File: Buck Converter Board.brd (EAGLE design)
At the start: 132.3 x 52 mm, 14 parts, among them J2 POWERPOLE_POWER25A_HORIZONTAL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, J3 POWERPOLE_POWER25A_HORIZONTAL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

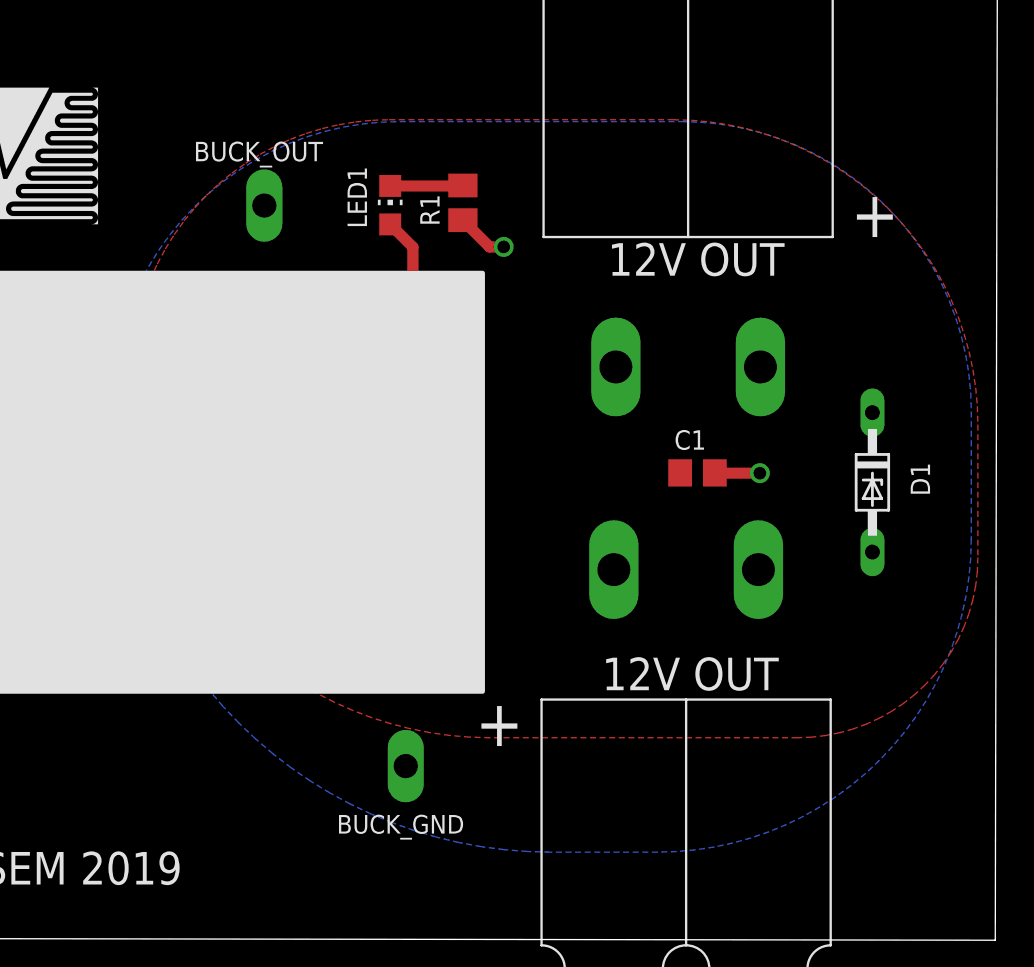
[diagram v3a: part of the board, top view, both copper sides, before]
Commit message: changed bypass cap on 555 to 22uF panasonic
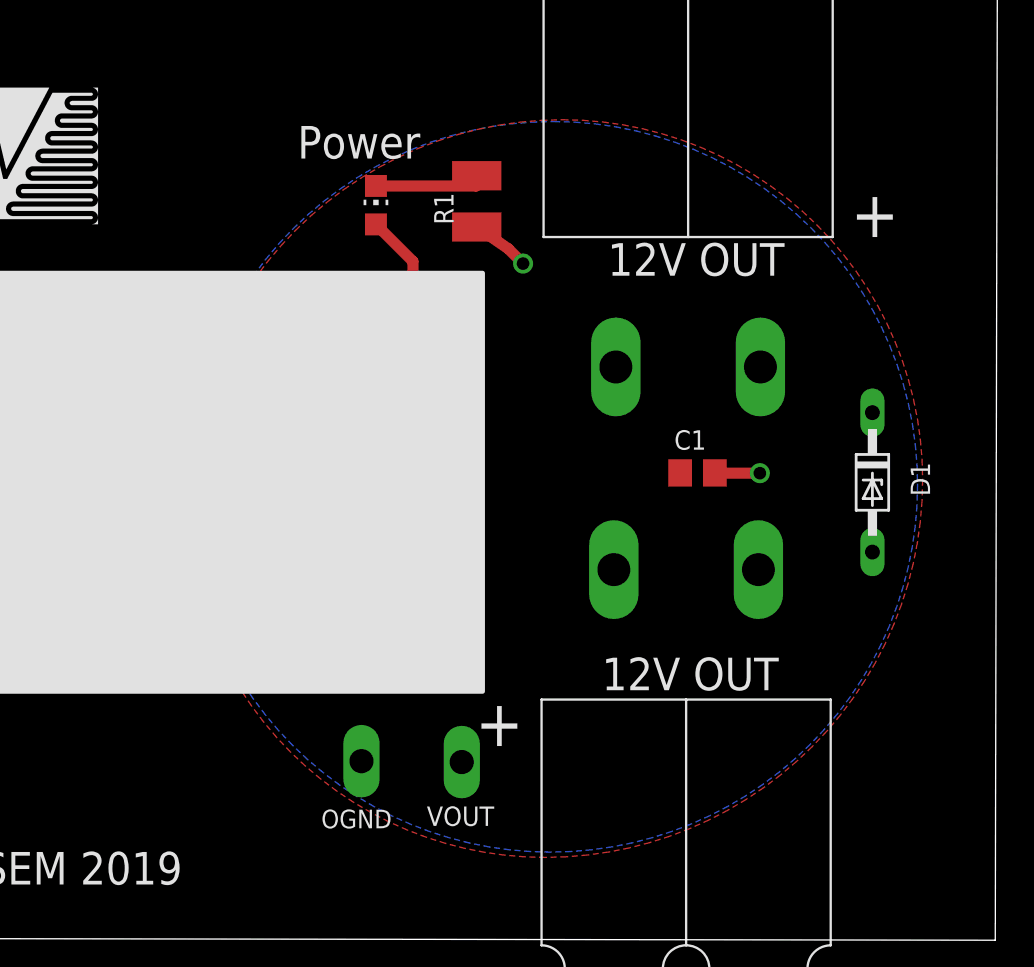
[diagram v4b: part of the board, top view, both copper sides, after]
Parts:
- removed BUCK_GND, BUCK_OUT: TEST_POINTSPAD1-13Y, master_library:P1-13Y
- added OGND, VOUT: TEST_POINTSPAD1-13Y, master_library:P1-13Y
- R1: device master_library:M0805 -> master_library:R3225
- moved LED1 0.78 mm to (87.2, 38.0)
- moved R1 0.76 mm to (92.7, 38.2)
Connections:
- net OGND: now also OGND.TP; no longer BUCK_GND.TP
- net V_OUT: now also VOUT.TP; no longer BUCK_OUT.TP
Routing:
- net N$1: track 3.98 -> 6.04 mm
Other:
- board text added: "Power"
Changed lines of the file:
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@@
 <text x="65.63" y="0.87" size="1.778" layer="25" font="vector">SEM 2019</text>
 <text x="119.94" y="-1.16" size="1.778" layer="26" rot="MR0">Louis Smidt</text>
+<text x="82.87" y="40.54" size="1.778" layer="25">Power</text>
 </plain>
 <attributes>
@@
 <attribute name="VALUE" x="19.71" y="43.78" size="0.0254" layer="27"/>
 </element>
-<element name="BUCK_OUT" library="master_library" package="P1-13Y" package3d_urn="urn:adsk.eagle:package:2274087/1" value="TEST_POINTSPAD1-13Y" x="81.06" y="37.97" smashed="yes">
-<attribute name="NAME" x="77.1978" y="40.3914" size="1.06" layer="25" ratio="10" rot="SR0"/>
-<attribute name="TP_SIGNAL_NAME" value="" x="79.79" y="34.16" size="1" layer="37"/>
-<attribute name="VALUE" x="78.66" y="36.44" size="0.0254" layer="27"/>
-</element>
-<element name="BUCK_GND" library="master_library" package="P1-13Y" package3d_urn="urn:adsk.eagle:package:2274087/1" value="TEST_POINTSPAD1-13Y" x="88.79" y="7.34" smashed="yes">
-<attribute name="NAME" x="85.0178" y="3.6514" size="1.016" layer="25" ratio="10" rot="SR0"/>
-<attribute name="TP_SIGNAL_NAME" value="" x="87.52" y="3.53" size="1" layer="37"/>
-<attribute name="VALUE" x="89.36" y="6.88" size="0.0254" layer="27"/>
+<element name="VOUT" library="master_library" package="P1-13Y" package3d_urn="urn:adsk.eagle:package:2274087/1" value="TEST_POINTSPAD1-13Y" x="91.85" y="7.56" smashed="yes">
+<attribute name="NAME" x="89.9378" y="4.0714" size="1.06" layer="25" ratio="10" rot="SR0"/>
+<attribute name="TP_SIGNAL_NAME" value="" x="90.58" y="3.75" size="1" layer="37"/>
+<attribute name="VALUE" x="89.45" y="6.03" size="0.0254" layer="27"/>
+</element>
+<element name="OGND" library="master_library" package="P1-13Y" package3d_urn="urn:adsk.eagle:package:2274087/1" value="TEST_POINTSPAD1-13Y" x="86.37" y="7.61" smashed="yes">
+<attribute name="NAME" x="84.1678" y="3.9414" size="1.016" layer="25" ratio="10" rot="SR0"/>
+<attribute name="TP_SIGNAL_NAME" value="" x="85.1" y="3.8" size="1" layer="37"/>
+<attribute name="VALUE" x="86.94" y="7.15" size="0.0254" layer="27"/>
 </element>
 <element name="BGND" library="master_library" package="P1-13Y" package3d_urn="urn:adsk.eagle:package:2274087/1" value="VBATT" x="28" y="14.92" smashed="yes">
@@
 <attribute name="VALUE" x="28" y="14.92" size="0.0254" layer="27"/>
 </element>
-<element name="LED1" library="led" library_urn="urn:adsk.eagle:library:259" package="CHIP-LED0805" package3d_urn="urn:adsk.eagle:package:15818/2" value="" x="87.94" y="37.99" smashed="yes">
-<attribute name="NAME" x="86.67" y="36.72" size="1.06" layer="25" rot="R90"/>
-<attribute name="VALUE" x="90.48" y="36.72" size="1.27" layer="27" rot="R90"/>
-</element>
-<element name="R1" library="master_library" package="M0805" package3d_urn="urn:adsk.eagle:package:2274058/1" value="470" x="91.91" y="38.12" smashed="yes" rot="R90">
-<attribute name="NAME" x="90.64" y="36.85" size="1.06" layer="25" rot="R90"/>
+<element name="LED1" library="led" library_urn="urn:adsk.eagle:library:259" package="CHIP-LED0805" package3d_urn="urn:adsk.eagle:package:15818/2" value="" x="87.16" y="37.99" smashed="yes">
+<attribute name="VALUE" x="89.7" y="36.72" size="1.27" layer="27" rot="R90"/>
+</element>
+<element name="R1" library="master_library" package="R3225" package3d_urn="urn:adsk.eagle:package:2274123/1" value="470" x="92.67" y="38.2" smashed="yes" rot="R90">
+<attribute name="NAME" x="91.4" y="36.93" size="1.06" layer="25" rot="R90"/>
 </element>
 </elements>
@@
 <contactref element="C1" pad="1"/>
 <polygon width="0.1524" layer="1">
-<vertex x="73.75875" y="28.5325" curve="-90"/>
-<vertex x="87.88625" y="42.66"/>
-<vertex x="103.39625" y="42.66" curve="-90"/>
-<vertex x="120.05375" y="26.0025"/>
-<vertex x="120.05375" y="18.74125" curve="-90"/>
-<vertex x="110.2025" y="8.89"/>
-<vertex x="93.40125" y="8.89" curve="-90"/>
+<vertex x="76.72375" y="22.0275" curve="-90"/>
+<vertex x="97.35625" y="42.66" curve="-90"/>
+<vertex x="117.03375" y="22.9825" curve="-90"/>
+<vertex x="96.40125" y="2.35" curve="-90"/>
 </polygon>
 <contactref element="D1" pad="C"/>
 <contactref element="UEE150W" pad="SNS+"/>
 <wire x1="89.18" y1="26.66" x2="89.18" y2="30.47" width="0.6096" layer="1"/>
-<contactref element="BUCK_OUT" pad="TP"/>
+<contactref element="VOUT" pad="TP"/>
 <contactref element="LED1" pad="A"/>
-<wire x1="89.18" y1="30.47" x2="89.18" y2="35.7" width="0.6096" layer="1"/>
-<wire x1="89.18" y1="35.7" x2="87.94" y2="36.94" width="0.6096" layer="1"/>
+<wire x1="89.18" y1="30.47" x2="89.18" y2="34.92" width="0.6096" layer="1"/>
+<wire x1="89.18" y1="34.92" x2="87.16" y2="36.94" width="0.6096" layer="1"/>
 </signal>
 <signal name="OGND" airwireshidden="yes">
@@
 <contactref element="UEE150W" pad="V_OUT-"/>
 <polygon width="0.1524" layer="16">
-<vertex x="72.616875" y="26.715625" curve="-90"/>
-<vertex x="88.46125" y="42.56"/>
-<vertex x="103.84875" y="42.56" curve="-90"/>
-<vertex x="119.69375" y="26.715"/>
-<vertex x="119.69375" y="19.76625" curve="-90"/>
-<vertex x="102.5675" y="2.64"/>
+<vertex x="76.771875" y="22.560625" curve="-90"/>
+<vertex x="96.77125" y="42.56"/>
+<vertex x="96.9" y="42.56" curve="-90"/>
+<vertex x="116.75625" y="22.70375" curve="-90"/>
 <vertex x="96.6925" y="2.64" curve="-90"/>
 </polygon>
@@
 <contactref element="UEE150W" pad="SNS-"/>
 <wire x1="89.18" y1="19.04" x2="89.18" y2="15.23" width="0.6096" layer="1"/>
-<contactref element="BUCK_GND" pad="TP"/>
+<contactref element="OGND" pad="TP"/>
 <contactref element="R1" pad="1"/>
-<wire x1="91.91" y1="37.17" x2="93.37" y2="35.71" width="0.6096" layer="1"/>
-<wire x1="93.37" y1="35.71" x2="94.14" y2="35.71" width="0.6096" layer="1"/>
-<via x="94.14" y="35.71" extent="1-16" drill="0.69"/>
+<wire x1="92.67" y1="36.8" x2="94.389553125" y2="35.610446875" width="0.6096" layer="1"/>
+<via x="95.2" y="34.8" extent="1-16" drill="0.69"/>
+<wire x1="94.389553125" y1="35.610446875" x2="95.2" y2="34.8" width="0.6096" layer="1"/>
 </signal>
 <signal name="N$1">
 <contactref element="LED1" pad="C"/>
 <contactref element="R1" pad="2"/>
-<wire x1="87.94" y1="39.04" x2="91.88" y2="39.04" width="0.6096" layer="1"/>
-<wire x1="91.88" y1="39.04" x2="91.91" y2="39.07" width="0.6096" layer="1"/>
+<wire x1="87.16" y1="39.04" x2="92.635" y2="39.04" width="0.6096" layer="1"/>
+<wire x1="92.635" y1="39.04" x2="92.67" y2="39.6" width="0.6096" layer="1"/>
 </signal>
 </signals>

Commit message: changed
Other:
- board size 132.3 x 52 mm -> 132.3 x 51.9 mm
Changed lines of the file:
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@@
 <layer number="43" name="vRestrict" color="2" fill="10" visible="yes" active="yes"/>
 <layer number="44" name="Drills" color="7" fill="1" visible="no" active="yes"/>
-<layer number="45" name="Holes" color="7" fill="1" visible="no" active="yes"/>
+<layer number="45" name="Holes" color="7" fill="1" visible="yes" active="yes"/>
 <layer number="46" name="Milling" color="3" fill="1" visible="no" active="yes"/>
 <layer number="47" name="Measures" color="7" fill="1" visible="no" active="yes"/>
@@
 <board>
 <plain>
-<wire x1="-11.23625" y1="-1.975" x2="121.00375" y2="-2.175" width="0" layer="20"/>
+<wire x1="-11.23625" y1="-2.095" x2="121.00375" y2="-2.175" width="0" layer="20"/>
 <wire x1="121.00375" y1="-2.175" x2="121.11375" y2="49.61875" width="0" layer="20"/>
-<wire x1="121.11375" y1="49.61875" x2="-11.12625" y2="49.81875" width="0" layer="20"/>
-<wire x1="-11.12625" y1="49.81875" x2="-11.23625" y2="-1.975" width="0" layer="20"/>
+<wire x1="121.11375" y1="49.61875" x2="-11.12625" y2="49.69875" width="0" layer="20"/>
+<wire x1="-11.12625" y1="49.69875" x2="-11.23625" y2="-2.095" width="0" layer="20"/>
 <text x="-7.15375" y="27.37625" size="1.778" layer="25" rot="R270">48V IN</text>
 <text x="109.48375" y="35.915" size="1.778" layer="25" rot="R180">12V OUT</text>
 <text x="109.16625" y="13.26375" size="1.778" layer="25" rot="R180">12V OUT</text>
-<text x="44.40125" y="0.70125" size="2.54" layer="25">REVolution</text>
+<text x="43.08125" y="-1.81875" size="2.54" layer="25">REVolution</text>
 <rectangle x1="52.405" y1="36.945" x2="54.475" y2="36.955" layer="25"/>
 <rectangle x1="56.685" y1="36.945" x2="57.185" y2="36.955" layer="25"/>
@@
 <rectangle x1="71.695" y1="44.405" x2="71.975" y2="44.415" layer="25"/>
 <text x="50.55" y="36.9" size="0.02" layer="25" font="vector">/Users/louissmidt/Downloads/Untitled-1.BMP</text>
-<text x="65.63" y="0.87" size="1.778" layer="25" font="vector">SEM 2019</text>
-<text x="119.94" y="-1.16" size="1.778" layer="26" rot="MR0">Louis Smidt</text>
+<text x="65.39" y="-1.77" size="1.778" layer="25" font="vector">SEM 2019</text>
+<text x="-0.34" y="-1.76" size="1.778" layer="25">Louis Smidt</text>
 <text x="82.87" y="40.54" size="1.778" layer="25">Power</text>
+<hole x="-4.92" y="45.43" drill="2"/>
+<hole x="-4.56" y="1.68" drill="2"/>
+<hole x="116.68" y="45.31" drill="2"/>
+<hole x="116.56" y="2.16" drill="2"/>
 </plain>
 <attributes>
